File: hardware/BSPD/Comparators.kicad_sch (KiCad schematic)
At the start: 22 parts, among them U4 LM393B, U6 74HC3G14, U7 LM393B, U9 74HC1G32GV

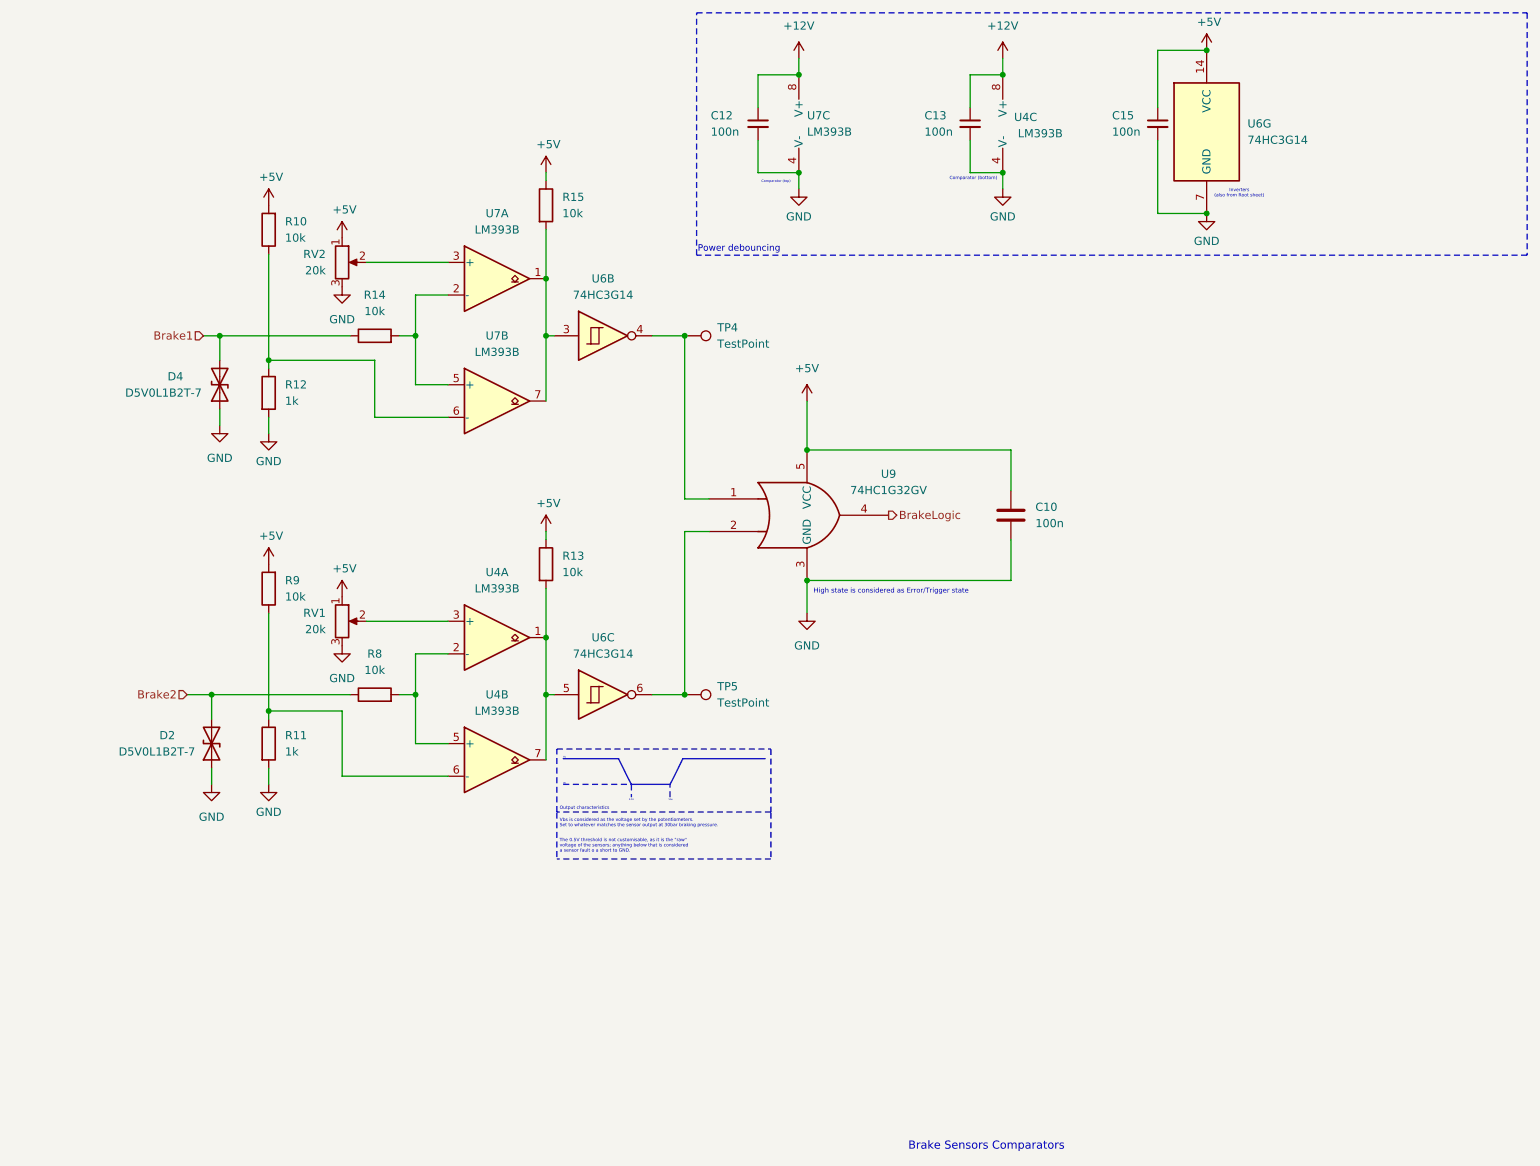
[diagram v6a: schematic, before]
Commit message: Minor changes + reassigned inverters
Inverters changed to 2 dual packaged, since one more inverter appeared, and there was no quad inverter from chosen series.
Placed TestPoints more sensically
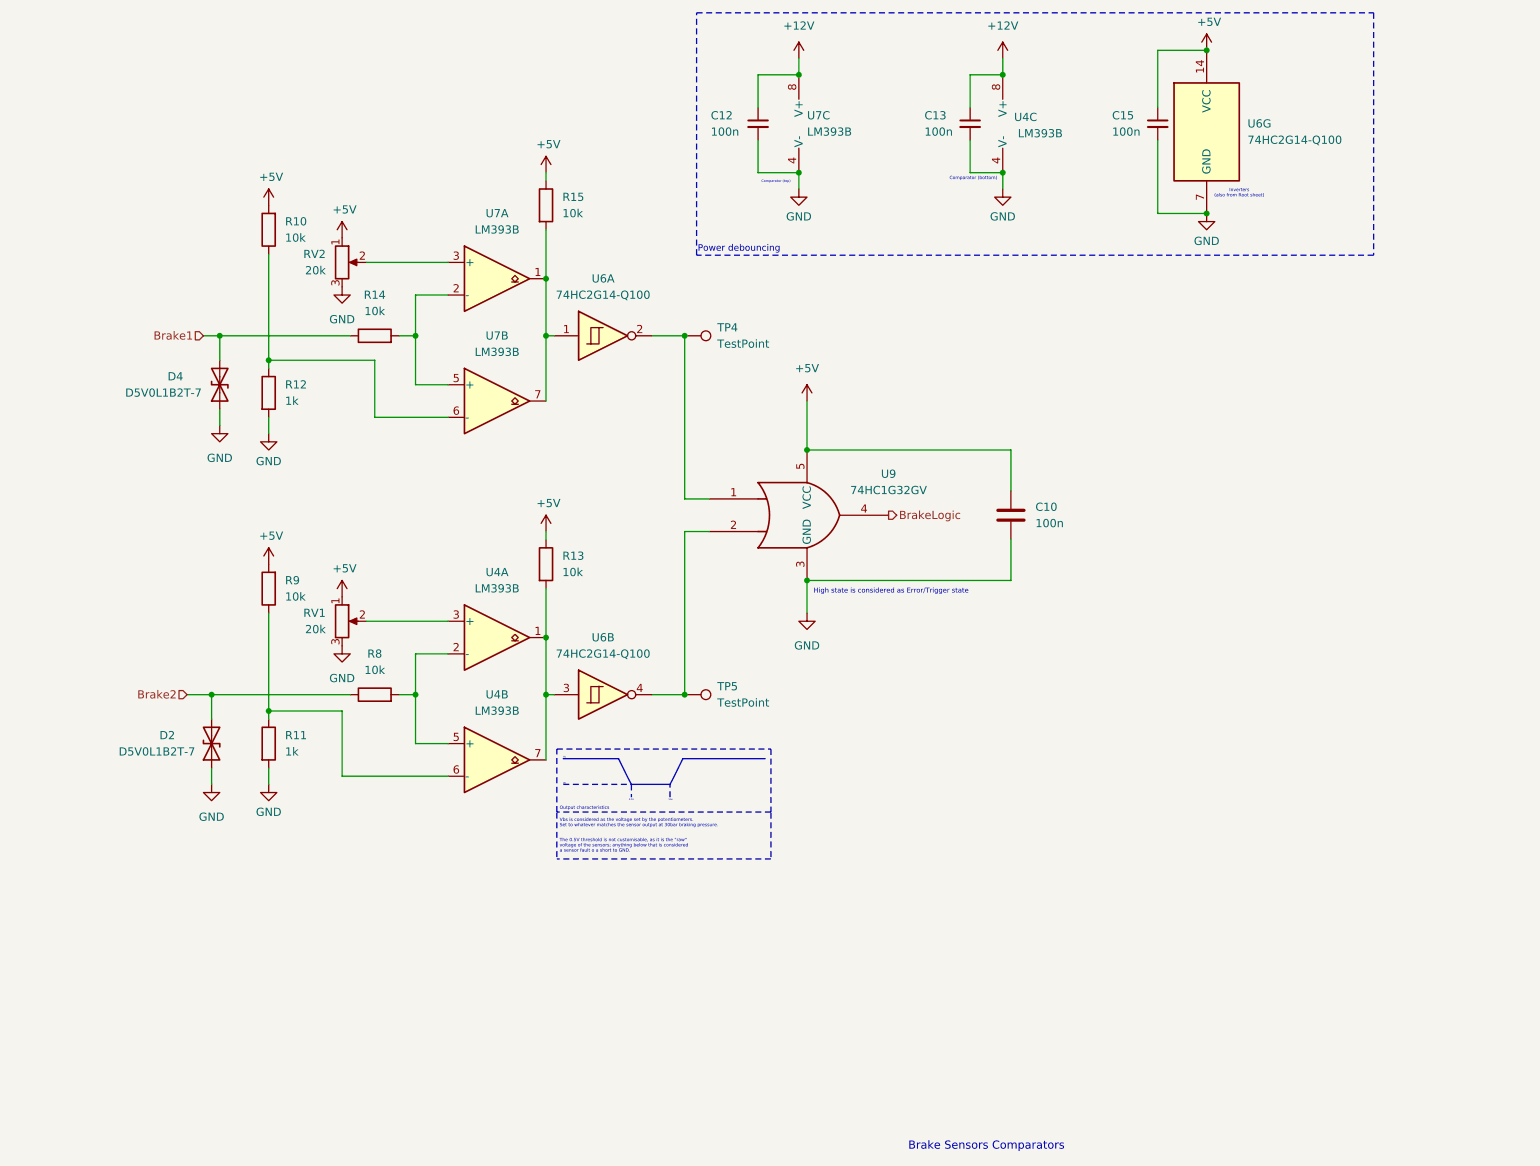
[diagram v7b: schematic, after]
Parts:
- U6: value 74HC3G14 -> 74HC2G14-Q100
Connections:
- net at R15.2, U7.1, U7.7: now also U6.1; no longer U6.3
- net at TP4.1, U9.1: now also U6.2; no longer U6.4
- net at TP5.1, U9.2: now also U6.4; no longer U6.6
- net at R13.2, U4.1, U4.7: now also U6.3; no longer U6.5
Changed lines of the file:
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@@
 	(rectangle
 		(start 154.2541 13.2132)
-		(end 283.5833 50.9509)
+		(end 259.6795 50.9509)
 		(stroke
 			(width 0)
@@
 		(lib_id "74xx:74HC14")
 		(at 139.7 63.5 0)
-		(unit 2)
+		(unit 1)
 		(exclude_from_sim no)
 		(in_bom yes)
@@
 			)
 		)
-		(property "Value" "74HC3G14"
+		(property "Value" "74HC2G14-Q100"
 			(at 139.7 57.15 0)
 			(effects
@@
 			)
 		)
-		(property "Datasheet" "https://assets.nexperia.com/documents/data-sheet/74HC_HCT3G14.pdf"
+		(property "Datasheet" "https://assets.nexperia.com/documents/data-sheet/74HC_HCT2G14_Q100.pdf"
 			(at 139.7 63.5 0)
 			(effects
@@
 				(path "/b652b05a-4e3d-4ad1-b032-18886abe7d45/743c9fc1-2f1a-4d5a-9140-72b33986ce8b"
 					(reference "U6")
-					(unit 2)
+					(unit 1)
 				)
 			)
@@
 		(lib_id "74xx:74HC14")
 		(at 139.7 119.38 0)
-		(unit 3)
+		(unit 2)
 		(exclude_from_sim no)
 		(in_bom yes)
@@
 			)
 		)
-		(property "Value" "74HC3G14"
+		(property "Value" "74HC2G14-Q100"
 			(at 139.7 113.03 0)
 			(effects
@@
 			)
 		)
-		(property "Datasheet" "https://assets.nexperia.com/documents/data-sheet/74HC_HCT3G14.pdf"
+		(property "Datasheet" "https://assets.nexperia.com/documents/data-sheet/74HC_HCT2G14_Q100.pdf"
 			(at 139.7 119.38 0)
 			(effects
@@
 				(path "/b652b05a-4e3d-4ad1-b032-18886abe7d45/743c9fc1-2f1a-4d5a-9140-72b33986ce8b"
 					(reference "U6")
-					(unit 3)
+					(unit 2)
 				)
 			)
@@
 			)
 		)
-		(property "Value" "74HC3G14"
+		(property "Value" "74HC2G14-Q100"
 			(at 240.03 33.0199 0)
 			(effects
@@
 			)
 		)
-		(property "Datasheet" "https://assets.nexperia.com/documents/data-sheet/74HC_HCT3G14.pdf"
+		(property "Datasheet" "https://assets.nexperia.com/documents/data-sheet/74HC_HCT2G14_Q100.pdf"
 			(at 233.68 31.75 0)
 			(effects

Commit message: Assigned footprints
Harwin connectors not yet assigned!
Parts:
- C12, C13, C15: footprint (none) -> Capacitor_SMD:C_0603_1608Metric
- R10, R11, R12, R13, R14, R15, R8, R9: footprint (none) -> Resistor_SMD:R_0603_1608Metric
- RV1, RV2: footprint (none) -> Potentiometer_THT:Potentiometer_Bourns_3296W_Vertical
- U4, U7: footprint (none) -> Package_SO:VSSOP-8_3x3mm_P0.65mm
- U6: footprint (none) -> Package_TO_SOT_SMD:SOT-23-6
- U9: footprint (none) -> Package_TO_SOT_SMD:SOT-23-5
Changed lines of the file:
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@@
 			)
 		)
-		(property "Footprint" ""
+		(property "Footprint" "Resistor_SMD:R_0603_1608Metric"
 			(at 129.032 43.18 90)
 			(effects
@@
 			)
 		)
-		(property "Footprint" ""
+		(property "Footprint" "Package_SO:VSSOP-8_3x3mm_P0.65mm"
 			(at 172.72 30.48 0)
 			(effects
@@
 			)
 		)
-		(property "Datasheet" "http://ww1.microchip.com/downloads/en/DeviceDoc/MCP6566-6R-6U-7-9-1.8V-Low-Power-Open-Drain-Output-Comparator-DS20002143G.pdf"
+		(property "Datasheet" "https://www.ti.com/lit/ds/symlink/lm393.pdf"
 			(at 172.72 30.48 0)
 			(effects
@@
 			)
 		)
-		(property "Description" "Dual 1.8V Low-Power Open-Drain Output Comparator, SOIC-8/MSOP-8"
+		(property "Description" ""
 			(at 172.72 30.48 0)
 			(effects
@@
 			)
 		)
-		(property "Footprint" ""
+		(property "Footprint" "Resistor_SMD:R_0603_1608Metric"
 			(at 89.408 46.99 90)
 			(effects
@@
 			)
 		)
-		(property "Footprint" ""
+		(property "Footprint" "Package_SO:VSSOP-8_3x3mm_P0.65mm"
 			(at 123.19 54.61 0)
 			(effects
@@
 			)
 		)
-		(property "Datasheet" "http://ww1.microchip.com/downloads/en/DeviceDoc/MCP6566-6R-6U-7-9-1.8V-Low-Power-Open-Drain-Output-Comparator-DS20002143G.pdf"
+		(property "Datasheet" "https://www.ti.com/lit/ds/symlink/lm393.pdf"
 			(at 123.698 62.738 0)
 			(effects
@@
 			)
 		)
-		(property "Description" "Dual 1.8V Low-Power Open-Drain Output Comparator, SOIC-8/MSOP-8"
+		(property "Description" ""
 			(at 123.698 62.738 0)
 			(effects
@@
 			)
 		)
-		(property "Footprint" ""
+		(property "Footprint" "Resistor_SMD:R_0603_1608Metric"
 			(at 85.852 72.39 90)
 			(effects
@@
 			)
 		)
-		(property "Footprint" ""
+		(property "Footprint" "Package_TO_SOT_SMD:SOT-23-5"
 			(at 171.45 91.44 0)
 			(effects
@@
 			)
 		)
-		(property "Footprint" ""
+		(property "Footprint" "Package_SO:VSSOP-8_3x3mm_P0.65mm"
 			(at 123.19 110.49 0)
 			(effects
@@
 			)
 		)
-		(property "Datasheet" "http://ww1.microchip.com/downloads/en/DeviceDoc/MCP6566-6R-6U-7-9-1.8V-Low-Power-Open-Drain-Output-Comparator-DS20002143G.pdf"
+		(property "Datasheet" "https://www.ti.com/lit/ds/symlink/lm393.pdf"
 			(at 123.698 118.618 0)
 			(effects
@@
 			)
 		)
-		(property "Description" "Dual 1.8V Low-Power Open-Drain Output Comparator, SOIC-8/MSOP-8"
+		(property "Description" ""
 			(at 123.698 118.618 0)
 			(effects
@@
 			)
 		)
-		(property "Footprint" ""
+		(property "Footprint" "Capacitor_SMD:C_0603_1608Metric"
 			(at 163.83 30.48 0)
 			(effects
@@
 			)
 		)
-		(property "Footprint" ""
+		(property "Footprint" "Package_SO:VSSOP-8_3x3mm_P0.65mm"
 			(at 204.47 30.48 0)
 			(effects
@@
 			)
 		)
-		(property "Datasheet" "http://ww1.microchip.com/downloads/en/DeviceDoc/MCP6566-6R-6U-7-9-1.8V-Low-Power-Open-Drain-Output-Comparator-DS20002143G.pdf"
+		(property "Datasheet" "https://www.ti.com/lit/ds/symlink/lm393.pdf"
 			(at 204.978 38.608 0)
 			(effects
@@
 			)
 		)
-		(property "Description" "Dual 1.8V Low-Power Open-Drain Output Comparator, SOIC-8/MSOP-8"
+		(property "Description" ""
 			(at 204.978 38.608 0)
 			(effects
@@
 			)
 		)
-		(property "Footprint" ""
+		(property "Footprint" "Capacitor_SMD:C_0603_1608Metric"
 			(at 196.85 30.48 0)
 			(effects
@@
 			)
 		)
-		(property "Footprint" ""
+		(property "Footprint" "Potentiometer_THT:Potentiometer_Bourns_3296W_Vertical"
 			(at 99.06 52.07 0)
 			(effects
@@
 			)
 		)
-		(property "Footprint" ""
+		(property "Footprint" "Resistor_SMD:R_0603_1608Metric"
 			(at 104.14 65.278 90)
 			(effects
@@
 			)
 		)
-		(property "Footprint" ""
+		(property "Footprint" "Package_TO_SOT_SMD:SOT-23-6"
 			(at 139.7 63.5 0)
 			(effects
@@
 			)
 		)
-		(property "Footprint" ""
+		(property "Footprint" "Package_TO_SOT_SMD:SOT-23-6"
 			(at 139.7 119.38 0)
 			(effects
@@
 			)
 		)
-		(property "Footprint" ""
+		(property "Footprint" "Package_SO:VSSOP-8_3x3mm_P0.65mm"
 			(at 123.19 129.54 0)
 			(effects
@@
 			)
 		)
-		(property "Datasheet" "http://ww1.microchip.com/downloads/en/DeviceDoc/MCP6566-6R-6U-7-9-1.8V-Low-Power-Open-Drain-Output-Comparator-DS20002143G.pdf"
+		(property "Datasheet" "https://www.ti.com/lit/ds/symlink/lm393.pdf"
 			(at 123.698 137.668 0)
 			(effects
@@
 			)
 		)
-		(property "Description" "Dual 1.8V Low-Power Open-Drain Output Comparator, SOIC-8/MSOP-8"
+		(property "Description" ""
 			(at 123.698 137.668 0)
 			(effects
@@
 			)
 		)
-		(property "Footprint" ""
+		(property "Footprint" "Capacitor_SMD:C_0603_1608Metric"
 			(at 226.06 30.48 0)
 			(effects
@@
 			)
 		)
-		(property "Footprint" ""
+		(property "Footprint" "Potentiometer_THT:Potentiometer_Bourns_3296W_Vertical"
 			(at 99.06 107.95 0)
 			(effects
@@
 			)
 		)
-		(property "Footprint" ""
+		(property "Footprint" "Resistor_SMD:R_0603_1608Metric"
 			(at 129.032 99.06 90)
 			(effects
@@
 			)
 		)
-		(property "Footprint" ""
+		(property "Footprint" "Resistor_SMD:R_0603_1608Metric"
 			(at 104.14 121.158 90)
 			(effects
@@
 			)
 		)
-		(property "Footprint" ""
+		(property "Footprint" "Package_SO:VSSOP-8_3x3mm_P0.65mm"
 			(at 123.19 73.66 0)
 			(effects
@@
 			)
 		)
-		(property "Datasheet" "http://ww1.microchip.com/downloads/en/DeviceDoc/MCP6566-6R-6U-7-9-1.8V-Low-Power-Open-Drain-Output-Comparator-DS20002143G.pdf"
+		(property "Datasheet" "https://www.ti.com/lit/ds/symlink/lm393.pdf"
 			(at 123.698 81.788 0)
 			(effects
@@
 			)
 		)
-		(property "Description" "Dual 1.8V Low-Power Open-Drain Output Comparator, SOIC-8/MSOP-8"
+		(property "Description" ""
 			(at 123.698 81.788 0)
 			(effects
@@
 			)
 		)
-		(property "Footprint" ""
+		(property "Footprint" "Resistor_SMD:R_0603_1608Metric"
 			(at 85.852 127 90)
 			(effects
@@
 			)
 		)
-		(property "Footprint" ""
+		(property "Footprint" "Package_TO_SOT_SMD:SOT-23-6"
 			(at 233.68 31.75 0)
 			(effects
@@
 			)
 		)
-		(property "Footprint" ""
+		(property "Footprint" "Resistor_SMD:R_0603_1608Metric"
 			(at 89.408 102.87 90)
 			(effects
